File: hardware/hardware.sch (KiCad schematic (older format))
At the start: 9 parts, among them P1 CONN_01X08, P2 CONN_01X08, P3 CONN_01X02

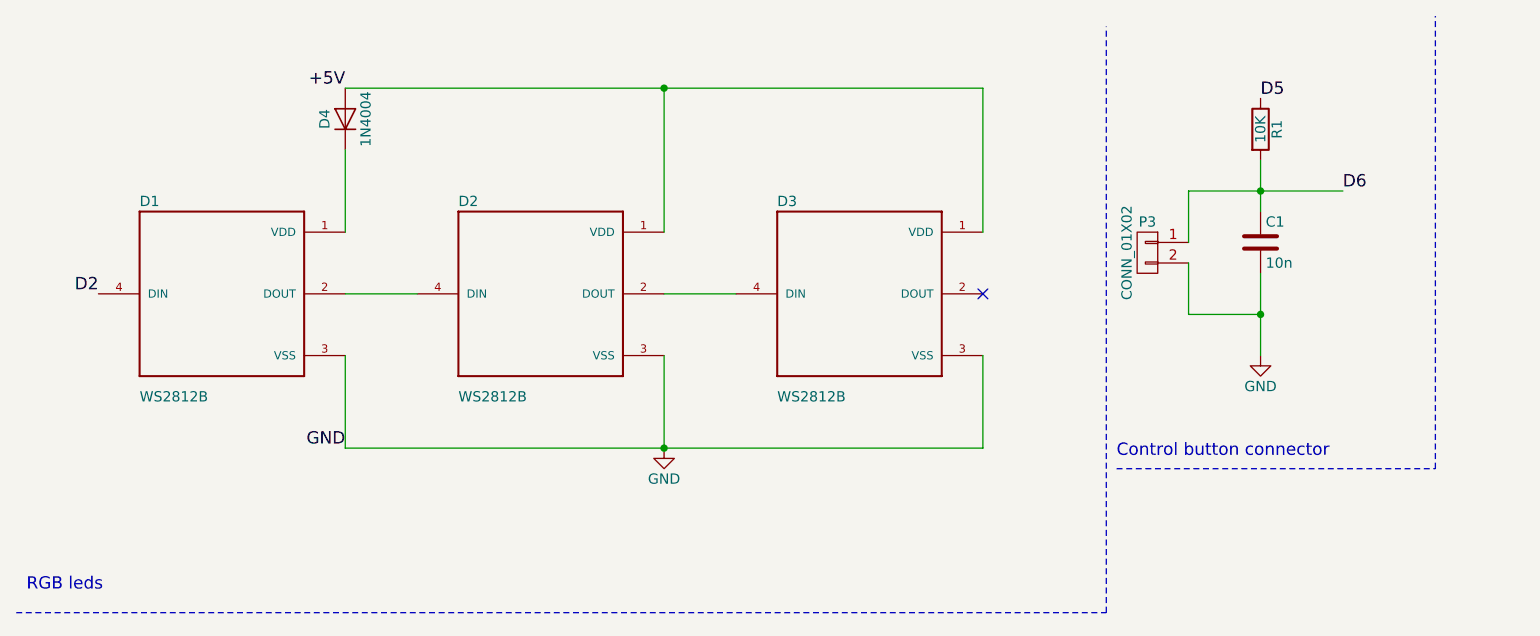
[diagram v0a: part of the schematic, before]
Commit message: 1st re-reading * serial resistor with DIN * decoupling capa for led power * D4 footprint
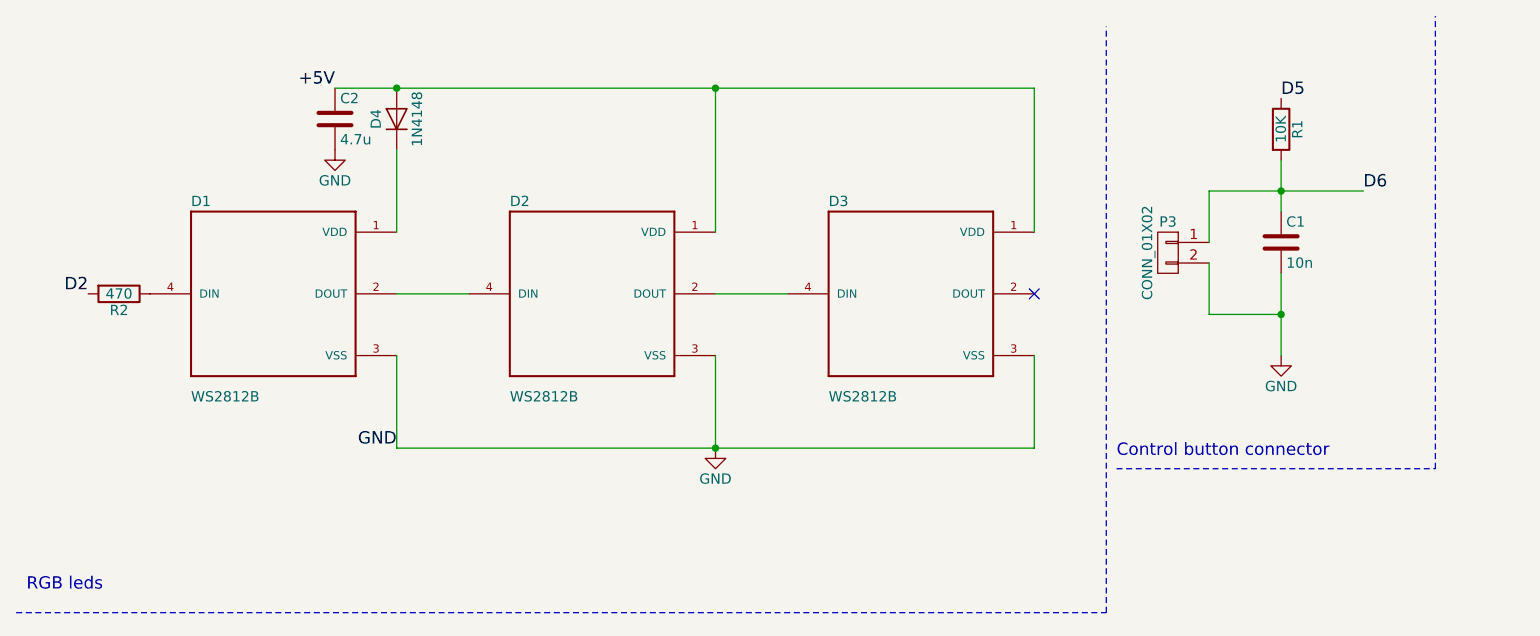
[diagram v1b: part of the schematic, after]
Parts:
- added C2: 4.7u, Capacitors_SMD:C_0402, symbol C
- added R2: 470, Resistors_SMD:R_0402, symbol R
- D4: value 1N4004 -> 1N4148; footprint Diodes_ThroughHole:Diode_DO-35_SOD27_Horizontal_RM10 -> Diodes_SMD:MiniMELF_Standard
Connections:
- net +5V: now also C2.1
- net D2: now also R2.2; no longer D1.4 (DIN)
- net GND: now also C2.2
- new net: D1.4 (DIN), R2.1
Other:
- moved on the sheet: C1, D1, D2, D3, D4, P3, R1
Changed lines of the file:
@@
 L WS2812B D1
 U 1 1 577173C5
-P 1500 1800
-F 0 "D1" H 1100 2250 50  0000 L CNN
-F 1 "WS2812B" H 1100 1300 50  0000 L CNN
-F 2 "WS2812B:LED_WS2812B" H 1500 1800 50  0001 L CNN
-F 3 "" H 1500 1800 60  0000 C CNN
-	1    1500 1800
+P 1750 1800
+F 0 "D1" H 1350 2250 50  0000 L CNN
+F 1 "WS2812B" H 1350 1300 50  0000 L CNN
+F 2 "WS2812B:LED_WS2812B" H 1750 1800 50  0001 L CNN
+F 3 "" H 1750 1800 60  0000 C CNN
+	1    1750 1800
 	1    0    0    -1
 $EndComp
@@
 L WS2812B D2
 U 1 1 577174D3
-P 3050 1800
-F 0 "D2" H 2650 2250 50  0000 L CNN
-F 1 "WS2812B" H 2650 1300 50  0000 L CNN
-F 2 "WS2812B:LED_WS2812B" H 3050 1800 50  0001 L CNN
-F 3 "" H 3050 1800 60  0000 C CNN
-	1    3050 1800
+P 3300 1800
+F 0 "D2" H 2900 2250 50  0000 L CNN
+F 1 "WS2812B" H 2900 1300 50  0000 L CNN
+F 2 "WS2812B:LED_WS2812B" H 3300 1800 50  0001 L CNN
+F 3 "" H 3300 1800 60  0000 C CNN
+	1    3300 1800
 	1    0    0    -1
 $EndComp
@@
 L WS2812B D3
 U 1 1 57717547
-P 4600 1800
-F 0 "D3" H 4200 2250 50  0000 L CNN
-F 1 "WS2812B" H 4200 1300 50  0000 L CNN
-F 2 "WS2812B:LED_WS2812B" H 4600 1800 50  0001 L CNN
-F 3 "" H 4600 1800 60  0000 C CNN
-	1    4600 1800
-	1    0    0    -1
-$EndComp
-Wire Wire Line
-	3650 1800 4000 1800
-Wire Wire Line
-	2100 1800 2450 1800
+P 4850 1800
+F 0 "D3" H 4450 2250 50  0000 L CNN
+F 1 "WS2812B" H 4450 1300 50  0000 L CNN
+F 2 "WS2812B:LED_WS2812B" H 4850 1800 50  0001 L CNN
+F 3 "" H 4850 1800 60  0000 C CNN
+	1    4850 1800
+	1    0    0    -1
+$EndComp
+Wire Wire Line
+	3900 1800 4250 1800
+Wire Wire Line
+	2350 1800 2700 1800
 $Comp
 L D D4
 U 1 1 57717974
-P 2100 950
-F 0 "D4" H 2100 1050 50  0000 C CNN
-F 1 "1N4004" H 2100 850 50  0000 C CNN
-F 2 "Diodes_ThroughHole:Diode_DO-35_SOD27_Horizontal_RM10" H 2100 950 60  0001 C CNN
-F 3 "" H 2100 950 60  0000 C CNN
-	1    2100 950
+P 2350 950
+F 0 "D4" H 2350 1050 50  0000 C CNN
+F 1 "1N4148" H 2350 850 50  0000 C CNN
+F 2 "Diodes_SMD:MiniMELF_Standard" H 2350 950 60  0001 C CNN
+F 3 "" H 2350 950 60  0000 C CNN
+	1    2350 950
 	0    -1   -1   0
 $EndComp
 Wire Wire Line
-	2100 1500 2100 1100
-Wire Wire Line
-	2100 800  5200 800
-Wire Wire Line
-	3650 800  3650 1500
-Wire Wire Line
-	5200 800  5200 1500
-Connection ~ 3650 800
-Text Label 2100 800  2    60   ~ 0
+	2350 1500 2350 1100
+Wire Wire Line
+	2050 800  5450 800
+Wire Wire Line
+	3900 800  3900 1500
+Wire Wire Line
+	5450 800  5450 1500
+Connection ~ 3900 800
+Text Label 2050 800  2    60   ~ 0
 +5V
-NoConn ~ 5200 1800
-Wire Wire Line
-	2100 2100 2100 2550
-Wire Wire Line
-	2100 2550 5200 2550
-Wire Wire Line
-	3650 2550 3650 2100
-Wire Wire Line
-	5200 2550 5200 2100
-Connection ~ 3650 2550
-Text Label 2100 2550 2    60   ~ 0
+NoConn ~ 5450 1800
+Wire Wire Line
+	2350 2100 2350 2550
+Wire Wire Line
+	2350 2550 5450 2550
+Wire Wire Line
+	3900 2550 3900 2100
+Wire Wire Line
+	5450 2550 5450 2100
+Connection ~ 3900 2550
+Text Label 2350 2550 2    60   ~ 0
 GND
 $Comp
 L R R1
 U 1 1 57717D17
-P 6550 1000
-F 0 "R1" V 6630 1000 50  0000 C CNN
-F 1 "10K" V 6550 1000 50  0000 C CNN
-F 2 "Resistors_SMD:R_0402" V 6480 1000 30  0001 C CNN
-F 3 "" H 6550 1000 30  0000 C CNN
-	1    6550 1000
+P 6650 1000
+F 0 "R1" V 6730 1000 50  0000 C CNN
+F 1 "10K" V 6650 1000 50  0000 C CNN
+F 2 "Resistors_SMD:R_0402" V 6580 1000 30  0001 C CNN
+F 3 "" H 6650 1000 30  0000 C CNN
+	1    6650 1000
 	1    0    0    -1
 $EndComp
@@
 L C C1
 U 1 1 57717D66
-P 6550 1550
-F 0 "C1" H 6575 1650 50  0000 L CNN
-F 1 "10n" H 6575 1450 50  0000 L CNN
-F 2 "Capacitors_SMD:C_0402" H 6588 1400 30  0001 C CNN
-F 3 "" H 6550 1550 60  0000 C CNN
-	1    6550 1550
+P 6650 1550
+F 0 "C1" H 6675 1650 50  0000 L CNN
+F 1 "10n" H 6675 1450 50  0000 L CNN
+F 2 "Capacitors_SMD:C_0402" H 6688 1400 30  0001 C CNN
+F 3 "" H 6650 1550 60  0000 C CNN
+	1    6650 1550
 	1    0    0    -1
 $EndComp
@@
 	5800 3350 5800 500
 Wire Wire Line
-	6550 1150 6550 1400
-Wire Wire Line
-	6200 1300 6950 1300
-Connection ~ 6550 1300
-Wire Wire Line
-	6550 1700 6550 2100
-Wire Wire Line
-	6550 1900 6200 1900
-Connection ~ 6550 1900
+	6650 1150 6650 1400
+Wire Wire Line
+	6300 1300 7050 1300
+Connection ~ 6650 1300
+Wire Wire Line
+	6650 1700 6650 2100
+Wire Wire Line
+	6650 1900 6300 1900
+Connection ~ 6650 1900
 $Comp
 L GND #PWR05
 U 1 1 5771843C
-P 6550 2100
-F 0 "#PWR05" H 6550 1850 50  0001 C CNN
-F 1 "GND" H 6550 1950 50  0000 C CNN
-F 2 "" H 6550 2100 60  0000 C CNN
-F 3 "" H 6550 2100 60  0000 C CNN
-	1    6550 2100
+P 6650 2100
+F 0 "#PWR05" H 6650 1850 50  0001 C CNN
+F 1 "GND" H 6650 1950 50  0000 C CNN
+F 2 "" H 6650 2100 60  0000 C CNN
+F 3 "" H 6650 2100 60  0000 C CNN
+	1    6650 2100
 	1    0    0    -1
 $EndComp
@@
 L GND #PWR06
 U 1 1 5771848D
-P 3650 2550
-F 0 "#PWR06" H 3650 2300 50  0001 C CNN
-F 1 "GND" H 3650 2400 50  0000 C CNN
-F 2 "" H 3650 2550 60  0000 C CNN
-F 3 "" H 3650 2550 60  0000 C CNN
-	1    3650 2550
+P 3900 2550
+F 0 "#PWR06" H 3900 2300 50  0001 C CNN
+F 1 "GND" H 3900 2400 50  0000 C CNN
+F 2 "" H 3900 2550 60  0000 C CNN
+F 3 "" H 3900 2550 60  0000 C CNN
+	1    3900 2550
 	1    0    0    -1
 $EndComp
@@
 L CONN_01X02 P3
 U 1 1 577189A7
-P 6000 1600
-F 0 "P3" H 6000 1750 50  0000 C CNN
-F 1 "CONN_01X02" V 6100 1600 50  0000 C CNN
-F 2 "Connect:PINHEAD1-2" H 6000 1600 60  0001 C CNN
-F 3 "" H 6000 1600 60  0000 C CNN
-	1    6000 1600
+P 6100 1600
+F 0 "P3" H 6100 1750 50  0000 C CNN
+F 1 "CONN_01X02" V 6200 1600 50  0000 C CNN
+F 2 "Connect:PINHEAD1-2" H 6100 1600 60  0001 C CNN
+F 3 "" H 6100 1600 60  0000 C CNN
+	1    6100 1600
 	-1   0    0    -1
 $EndComp
 Wire Wire Line
-	6200 1300 6200 1550
-Wire Wire Line
-	6200 1900 6200 1650
-Text Label 900  1800 2    60   ~ 0
+	6300 1300 6300 1550
+Wire Wire Line
+	6300 1900 6300 1650
+Text Label 850  1800 2    60   ~ 0
 D2
-Text Label 6550 850  0    60   ~ 0
+Text Label 6650 850  0    60   ~ 0
 D5
-Text Label 6950 1300 0    60   ~ 0
+Text Label 7050 1300 0    60   ~ 0
 D6
 NoConn ~ 9450 1250
@@
 NoConn ~ 10300 1650
 NoConn ~ 10300 1750
+$Comp
+L R R2
+U 1 1 5772A62F
+P 1000 1800
+F 0 "R2" V 1080 1800 50  0000 C CNN
+F 1 "470" V 1000 1800 50  0000 C CNN
+F 2 "Resistors_SMD:R_0402" V 930 1800 30  0001 C CNN
+F 3 "" H 1000 1800 30  0000 C CNN
+	1    1000 1800
+	0    1    1    0
+$EndComp
+$Comp
+L C C2
+U 1 1 5772A7DC
+P 2050 950
+F 0 "C2" H 2075 1050 50  0000 L CNN
+F 1 "4.7u" H 2075 850 50  0000 L CNN
+F 2 "Capacitors_SMD:C_0402" H 2088 800 30  0001 C CNN
+F 3 "" H 2050 950 60  0000 C CNN
+	1    2050 950
+	1    0    0    -1
+$EndComp
+Connection ~ 2350 800
+$Comp
+L GND #PWR07
+U 1 1 5772A872
+P 2050 1100
+F 0 "#PWR07" H 2050 850 50  0001 C CNN
+F 1 "GND" H 2050 950 50  0000 C CNN
+F 2 "" H 2050 1100 60  0000 C CNN
+F 3 "" H 2050 1100 60  0000 C CNN
+	1    2050 1100
+	1    0    0    -1
+$EndComp
 $EndSCHEMATC

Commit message: 1st review : placement/routage
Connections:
- net D5: now also C1.1, P3.1 (P1), R1.2; no longer R1.1
- net D6: now also R1.1; no longer C1.1, P3.1 (P1), R1.2
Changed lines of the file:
@@
 Text Label 850  1800 2    60   ~ 0
 D2
+Text Label 7050 1300 0    60   ~ 0
+D5
 Text Label 6650 850  0    60   ~ 0
-D5
-Text Label 7050 1300 0    60   ~ 0
 D6
 NoConn ~ 9450 1250

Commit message: Move button input to 3.3V
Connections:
- net +3.3V: now also R1.1
- net D6: no longer R1.1
- no-connect marks 11 -> 12
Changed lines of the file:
@@
 Text Label 7050 1300 0    60   ~ 0
 D5
-Text Label 6650 850  0    60   ~ 0
-D6
 NoConn ~ 9450 1250
 NoConn ~ 9450 1350
@@
 	1    0    0    -1
 $EndComp
+Text Label 6650 850  0    60   ~ 0
++3.3V
+NoConn ~ 10300 1350
 $EndSCHEMATC

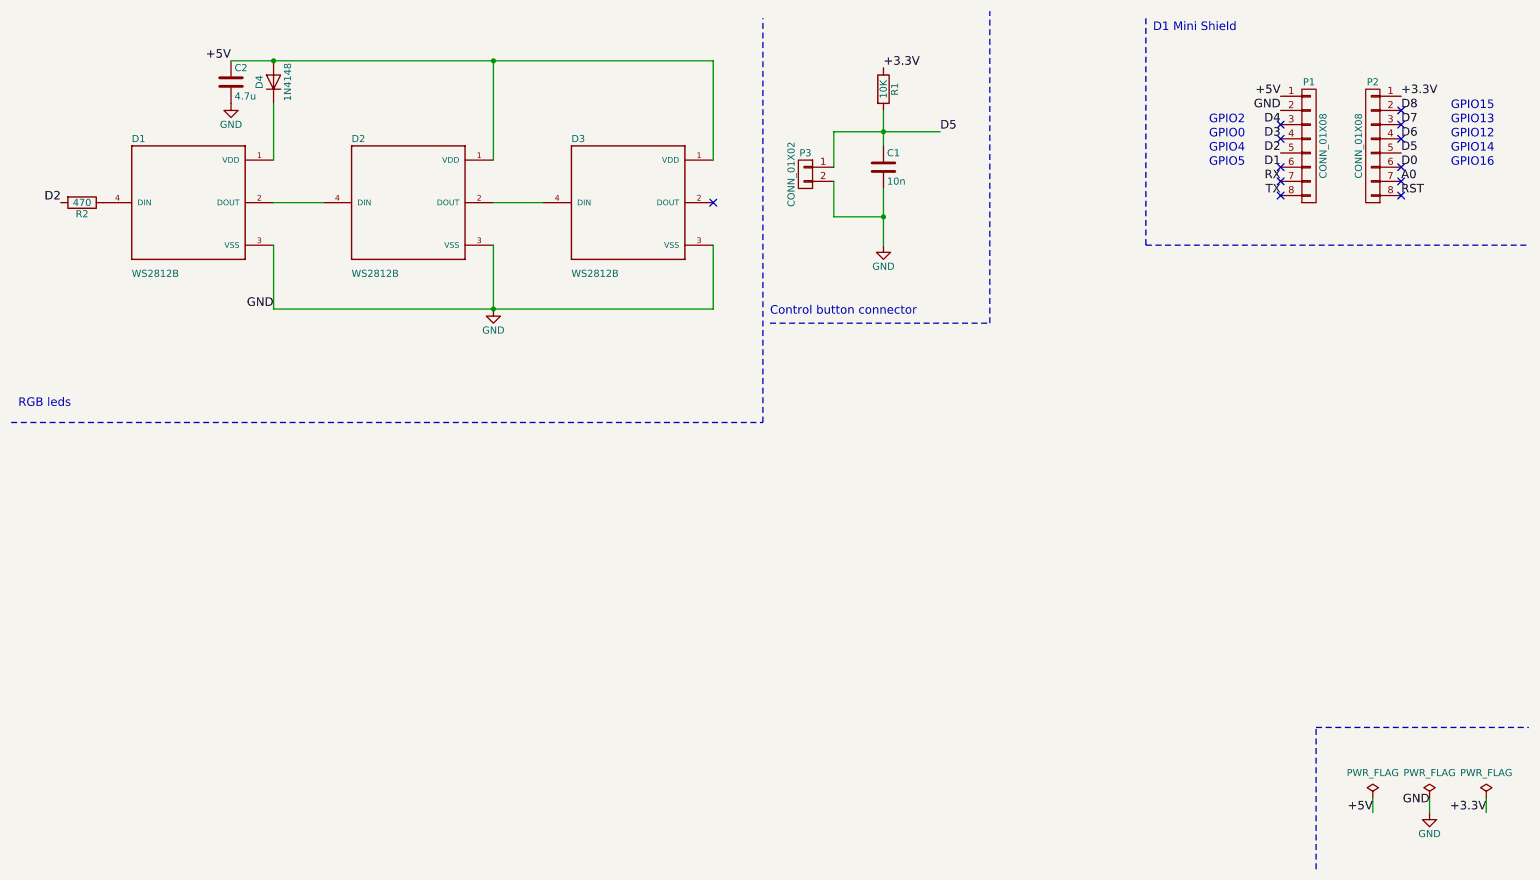
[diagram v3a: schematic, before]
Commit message: Add connector for led extensions
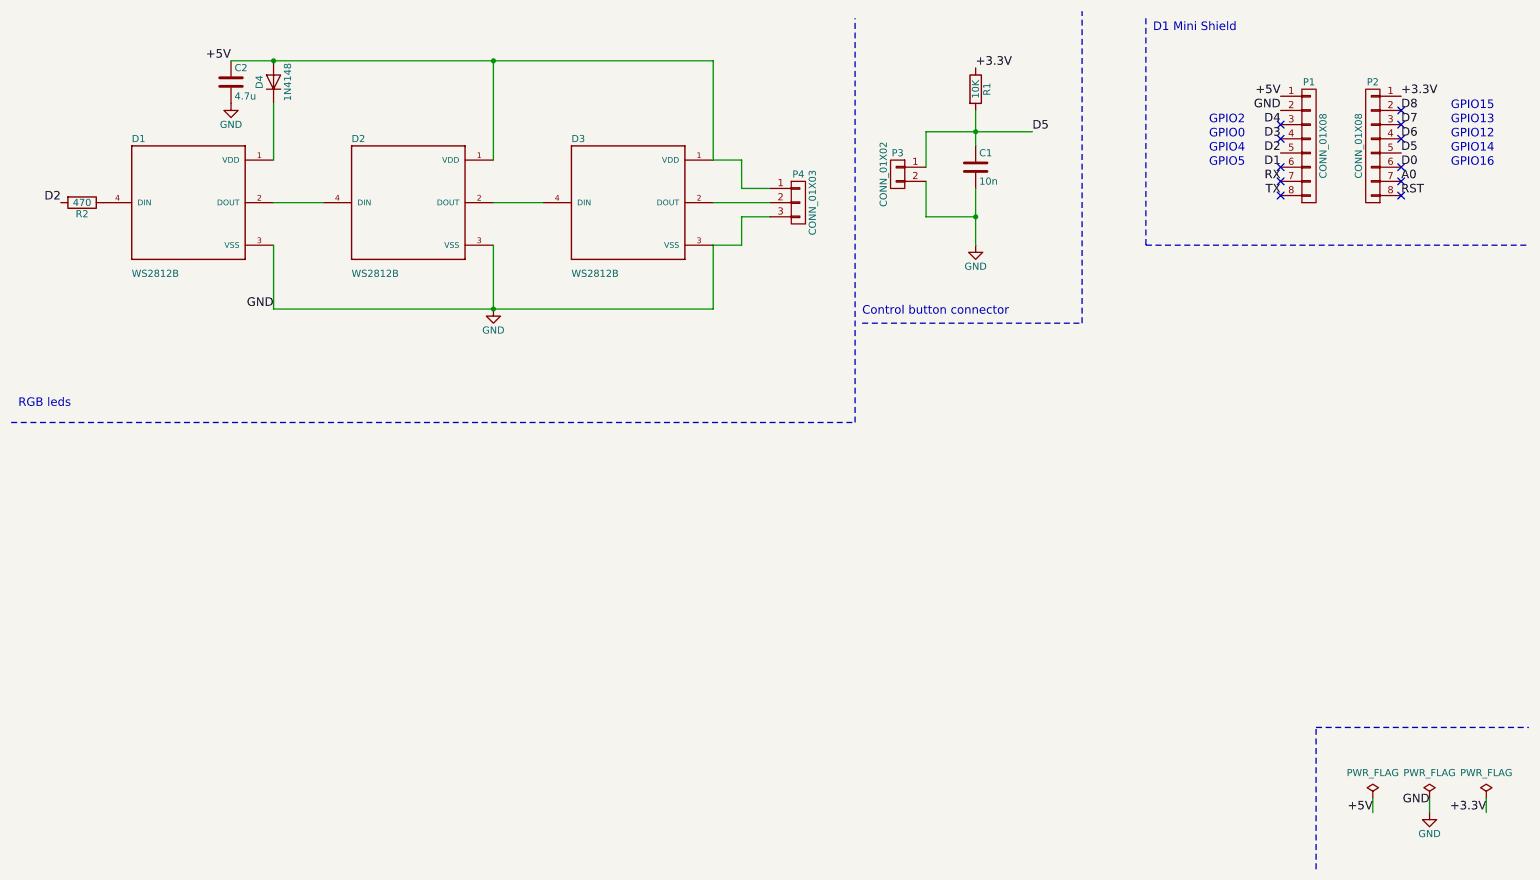
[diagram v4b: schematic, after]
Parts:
- added P4: CONN_01X03, Connect:PINHEAD1-3, symbol CONN_01X03
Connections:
- net +5V: now also P4.1 (P1)
- net GND: now also P4.3 (P3)
- net at D3.2 (DOUT): now also P4.2 (P2)
- no-connect marks 12 -> 11
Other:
- moved on the sheet: C1, P3, R1
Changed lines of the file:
@@
 Text Label 2050 800  2    60   ~ 0
 +5V
-NoConn ~ 5450 1800
 Wire Wire Line
 	2350 2100 2350 2550
@@
 L R R1
 U 1 1 57717D17
-P 6650 1000
-F 0 "R1" V 6730 1000 50  0000 C CNN
-F 1 "10K" V 6650 1000 50  0000 C CNN
-F 2 "Resistors_SMD:R_0402" V 6580 1000 30  0001 C CNN
-F 3 "" H 6650 1000 30  0000 C CNN
-	1    6650 1000
+P 7300 1000
+F 0 "R1" V 7380 1000 50  0000 C CNN
+F 1 "10K" V 7300 1000 50  0000 C CNN
+F 2 "Resistors_SMD:R_0402" V 7230 1000 30  0001 C CNN
+F 3 "" H 7300 1000 30  0000 C CNN
+	1    7300 1000
 	1    0    0    -1
 $EndComp
@@
 L C C1
 U 1 1 57717D66
-P 6650 1550
-F 0 "C1" H 6675 1650 50  0000 L CNN
-F 1 "10n" H 6675 1450 50  0000 L CNN
-F 2 "Capacitors_SMD:C_0402" H 6688 1400 30  0001 C CNN
-F 3 "" H 6650 1550 60  0000 C CNN
-	1    6650 1550
+P 7300 1550
+F 0 "C1" H 7325 1650 50  0000 L CNN
+F 1 "10n" H 7325 1450 50  0000 L CNN
+F 2 "Capacitors_SMD:C_0402" H 7338 1400 30  0001 C CNN
+F 3 "" H 7300 1550 60  0000 C CNN
+	1    7300 1550
 	1    0    0    -1
 $EndComp
@@
 	9700 5500 11200 5500
 Wire Notes Line
-	500  3350 5800 3350
-Wire Notes Line
-	5800 3350 5800 500
-Wire Wire Line
-	6650 1150 6650 1400
-Wire Wire Line
-	6300 1300 7050 1300
-Connection ~ 6650 1300
-Wire Wire Line
-	6650 1700 6650 2100
-Wire Wire Line
-	6650 1900 6300 1900
-Connection ~ 6650 1900
+	500  3350 6450 3350
+Wire Notes Line
+	6450 3350 6450 500
+Wire Wire Line
+	7300 1150 7300 1400
+Wire Wire Line
+	6950 1300 7700 1300
+Connection ~ 7300 1300
+Wire Wire Line
+	7300 1700 7300 2100
+Wire Wire Line
+	7300 1900 6950 1900
+Connection ~ 7300 1900
 $Comp
 L GND #PWR05
 U 1 1 5771843C
-P 6650 2100
-F 0 "#PWR05" H 6650 1850 50  0001 C CNN
-F 1 "GND" H 6650 1950 50  0000 C CNN
-F 2 "" H 6650 2100 60  0000 C CNN
-F 3 "" H 6650 2100 60  0000 C CNN
-	1    6650 2100
+P 7300 2100
+F 0 "#PWR05" H 7300 1850 50  0001 C CNN
+F 1 "GND" H 7300 1950 50  0000 C CNN
+F 2 "" H 7300 2100 60  0000 C CNN
+F 3 "" H 7300 2100 60  0000 C CNN
+	1    7300 2100
 	1    0    0    -1
 $EndComp
@@
 $EndComp
 Wire Notes Line
-	5850 2650 7400 2650
-Wire Notes Line
-	7400 2650 7400 450
+	6500 2650 8050 2650
+Wire Notes Line
+	8050 2650 8050 450
 Text Notes 550  3250 0    60   ~ 0
 RGB leds
-Text Notes 5850 2600 0    60   ~ 0
+Text Notes 6500 2600 0    60   ~ 0
 Control button connector
 $Comp
 L CONN_01X02 P3
 U 1 1 577189A7
-P 6100 1600
-F 0 "P3" H 6100 1750 50  0000 C CNN
-F 1 "CONN_01X02" V 6200 1600 50  0000 C CNN
-F 2 "Connect:PINHEAD1-2" H 6100 1600 60  0001 C CNN
-F 3 "" H 6100 1600 60  0000 C CNN
-	1    6100 1600
+P 6750 1600
+F 0 "P3" H 6750 1750 50  0000 C CNN
+F 1 "CONN_01X02" V 6850 1600 50  0000 C CNN
+F 2 "Connect:PINHEAD1-2" H 6750 1600 60  0001 C CNN
+F 3 "" H 6750 1600 60  0000 C CNN
+	1    6750 1600
 	-1   0    0    -1
 $EndComp
 Wire Wire Line
-	6300 1300 6300 1550
-Wire Wire Line
-	6300 1900 6300 1650
+	6950 1300 6950 1550
+Wire Wire Line
+	6950 1900 6950 1650
 Text Label 850  1800 2    60   ~ 0
 D2
-Text Label 7050 1300 0    60   ~ 0
+Text Label 7700 1300 0    60   ~ 0
 D5
 NoConn ~ 9450 1250
@@
 	1    0    0    -1
 $EndComp
-Text Label 6650 850  0    60   ~ 0
+Text Label 7300 850  0    60   ~ 0
 +3.3V
 NoConn ~ 10300 1350
+$Comp
+L CONN_01X03 P4
+U 1 1 5772F386
+P 6050 1800
+F 0 "P4" H 6050 2000 50  0000 C CNN
+F 1 "CONN_01X03" V 6150 1800 50  0000 C CNN
+F 2 "Connect:PINHEAD1-3" H 6050 1800 60  0001 C CNN
+F 3 "" H 6050 1800 60  0000 C CNN
+	1    6050 1800
+	1    0    0    -1
+$EndComp
+Wire Wire Line
+	5450 1500 5650 1500
+Wire Wire Line
+	5650 1500 5650 1700
+Wire Wire Line
+	5650 1700 5850 1700
+Wire Wire Line
+	5450 1800 5850 1800
+Wire Wire Line
+	5450 2100 5650 2100
+Wire Wire Line
+	5650 2100 5650 1900
+Wire Wire Line
+	5650 1900 5850 1900
 $EndSCHEMATC
